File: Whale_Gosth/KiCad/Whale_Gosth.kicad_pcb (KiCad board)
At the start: 2 copper layers, 129.5 x 78.7 mm, 20 parts

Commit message: jpeg
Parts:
- removed the REF** at (211.3, 114.8)
- moved REF** 116.9 mm to (211.3, 114.8)
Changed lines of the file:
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@@
     (links 58)
     (no_connects 0)
-    (area 87.300999 42.596999 216.991001 121.487001)
+    (area 65.302001 27.272 242.546 135.088)
     (thickness 1.6)
     (drawings 17)
     (tracks 302)
     (zones 0)
-    (modules 20)
+    (modules 19)
     (nets 39)
   )
@@
   )
   (module Wire_Pads:SolderWirePad_single_2mmDrill (layer F.Cu)
-    (at 95.123 127.635)
+    (at 211.328 114.808)
     (fp_text reference REF** (at 0 -3.81) (layer F.SilkS)
       (effects (font (size 1 1) (thickness 0.15)))
@@
     )
     (pad 1 thru_hole circle (at 0 0) (size 6 6) (drill 4) (layers *.Cu *.Mask))
-  )
-  (module Wire_Pads:SolderWirePad_single_2mmDrill (layer F.Cu)
-    (at 211.328 114.808)
-    (fp_text reference REF** (at 0 -3.81) (layer F.SilkS)
-      (effects (font (size 1 1) (thickness 0.15)))
-    )
-    (fp_text value Fix (at -0.635 3.81) (layer F.Fab)
-      (effects (font (size 1 1) (thickness 0.15)))
-    )
-    (pad 1 thru_hole circle (at 0 0) (size 4.50088 4.50088) (drill 1.99898) (layers *.Cu *.Mask))
   )
   (module Wire_Pads:SolderWirePad_single_2mmDrill (layer F.Cu)
@@
   (segment (start 151.130115 62.267901) (end 149.945491 63.414509) (width 0.4) (layer B.Cu) (net 14))
   (segment (start 164.084 61.722) (end 163.576 62.23) (width 0.4) (layer B.Cu) (net 14))
-  (segment (start 149.86 63.4238) (end 149.86 86.36) (width 0.4) (layer F.Cu) (net 14) (status 880000))
+  (segment (start 149.86 63.4238) (end 149.86 86.36) (width 0.4) (layer F.Cu) (net 14) (status 80000))
   (segment (start 168.9354 57.5818) (end 165.354 61.722) (width 0.4) (layer B.Cu) (net 14) (status 80000))
   (segment (start 165.354 61.722) (end 165.294429 61.807491) (width 0.4) (layer B.Cu) (net 14) (status 80000))

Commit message: pcb v1.0
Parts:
- removed Regu_5V1: Screw_Terminal_1x03, Connectors_Terminal_Blocks:TerminalBlock_bornier-3_P5.08mm
- added ?: logo_pitaya, riri:logo_pitaya, F.Cu at (159.8, 102.2)
- added EN: , Wire_Pads:SolderWirePad_single_2mmDrill, F.Cu at (183.0, 88.3)
- added GND: , Wire_Pads:SolderWirePad_single_2mmDrill, F.Cu at (188.3, 88.3)
- added V_in: , Wire_Pads:SolderWirePad_single_2mmDrill, F.Cu at (185.7, 88.3)
- added V_out: , Wire_Pads:SolderWirePad_single_2mmDrill, F.Cu at (191.0, 88.3)
- Buck_Converter: renamed from Buck_converter1; value BUCK-CONVERTER -> (none)
- IN 24V: renamed from IN_24V1
- OUT 24V: renamed from OUT_24V1
- WS_0, WS_1, WS_2, WS_3, WS_4, WS_5: value Screw_Terminal_1x03 -> (none)
- moved Fix 0.51 mm to (161.7, 69.1)
- renumbered REF** to Fix
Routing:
- net +24V: track 0.00 -> 36.8 mm
- net GND: track 222.1 -> 252.2 mm, vias 0 -> 1
- net Net-(ESP-G1-Pad19): track 69.2 -> 41.6 mm
- net WS4: track 115.1 -> 95.4 mm
- net Net-(Buck_converter1-Pad4): track 192.0 -> 193.3 mm
- net IO2: track 46.0 -> 46.2 mm, vias 2 -> 1
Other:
- board text added: "+"
- board text added: "-"
- board text added: "24V"
- board text added: "3v3"
- board text added: "5V"
- board text added: "5v"
- board text added: "ESP32-WROOM"
- board text added: "GND"
- board text added: "Made by Riri"
- board text added: "Regulateur 7V"
- board text added: "V 1.0"
- board text added: "Whale Gosth"
- board text added: "clk"
- board text added: "cmd"
- board text added: "en"
- board text added: "gnd"
- board text added: "io0"
- board text added: "io12"
- board text added: "io13"
- board text added: "io14"
- board text added: "io15"
- board text added: "io16"
- board text added: "io17"
- board text added: "io2"
- board text added: "io25"
- board text added: "io26"
- board text added: "io27"
- board text added: "io32"
- board text added: "io33"
- board text added: "io34"
- board text added: "io35"
- board text added: "io4"
- board text added: "rxd0"
- board text added: "sd0"
- board text added: "sd1"
- board text added: "sd2"
- board text added: "sd3"
- board text added: "svn"
- board text added: "svp"
- board text added: "txd0"

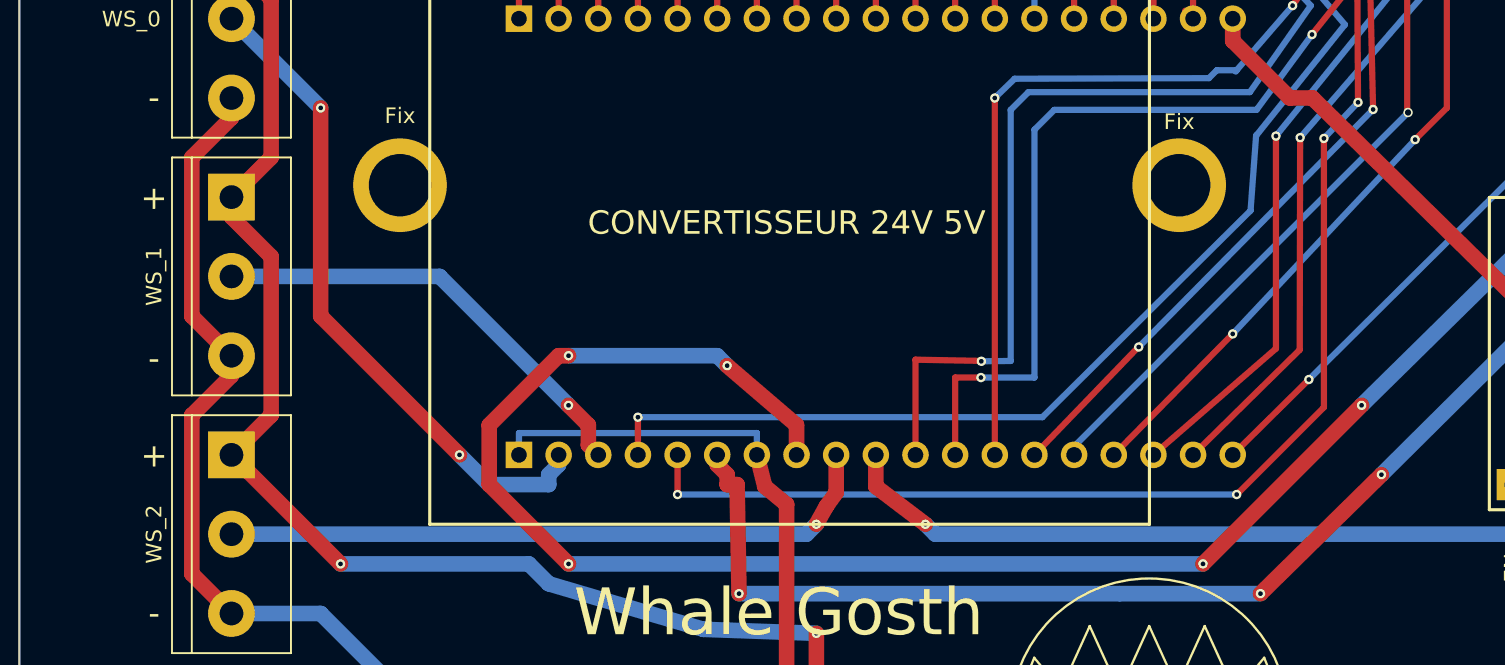
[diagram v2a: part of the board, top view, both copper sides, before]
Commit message: changer impreinte esp de 12 a 11 pas 2.54
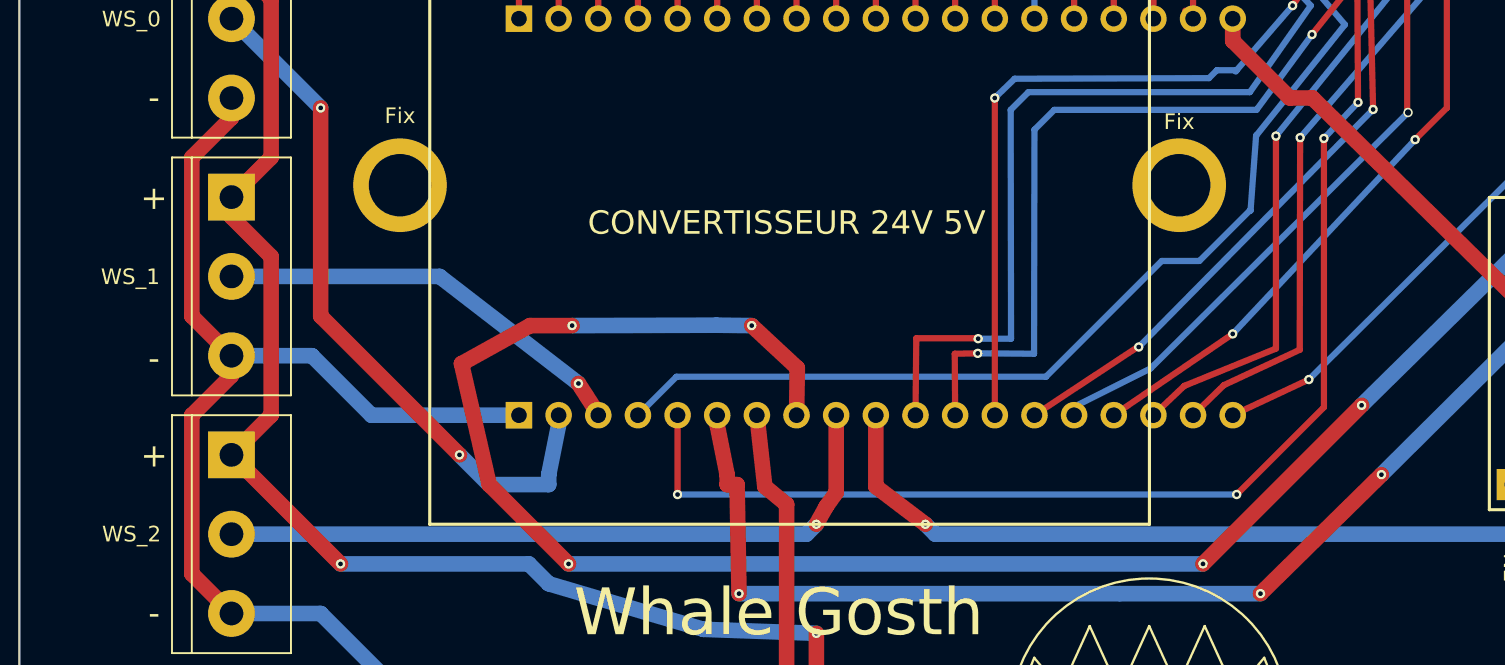
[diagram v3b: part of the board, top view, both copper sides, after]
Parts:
- moved ESP-D1 2.54 mm to (119.4, 83.8)
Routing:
- net WS5: track 135.6 -> 140.9 mm
- net GND: track 252.2 -> 256.7 mm
- net IO17: track 61.0 -> 58.4 mm
- net RXD0: track 90.4 -> 92.9 mm
- net WS3: track 65.0 -> 67.5 mm
- net WS2: track 42.5 -> 45.1 mm
- net IO4: track 53.9 -> 51.3 mm
- net IO16: track 59.2 -> 56.6 mm
- net WS4: track 95.4 -> 97.7 mm
- net WS0: track 42.7 -> 45.0 mm
- net TXDO: track 79.2 -> 77.4 mm
- net WS1: track 29.2 -> 27.4 mm
- net IO15: track 45.9 -> 44.3 mm
- net IO0: track 46.4 -> 44.8 mm
- net IO2: track 46.2 -> 44.7 mm
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
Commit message: angle droit
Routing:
- net WS0: track 45.0 -> 48.2 mm
- net IO16: track 56.6 -> 54.8 mm
- net SD1: track 44.4 -> 43.6 mm
- net WS5: track 140.9 -> 141.6 mm
- net Net-(Buck_converter1-Pad4): track 193.3 -> 194.1 mm
- net TXDO: track 77.4 -> 76.9 mm
